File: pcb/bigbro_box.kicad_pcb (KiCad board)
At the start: 2 copper layers, 100 x 58 mm, 54 parts, among them J1 Current Sense, J2 Display, J3 Mains, J4 Debug, J5 RFID, J6 Relay, J7 Ext, K1 G5LE-1, Q1 MMBT3904, Q2 MMBT3904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

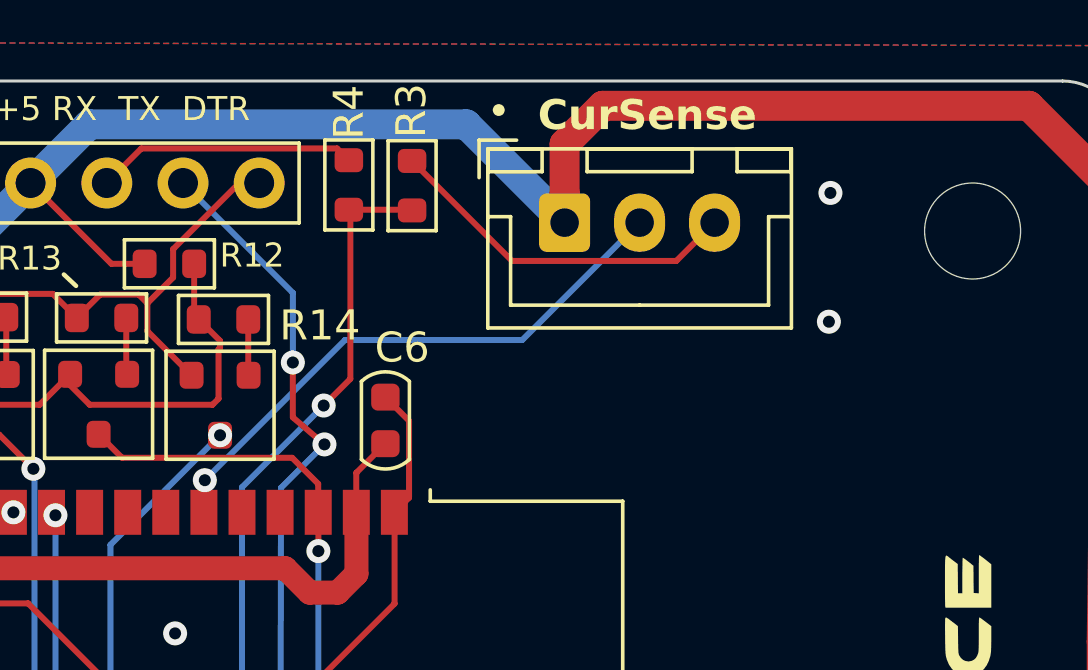
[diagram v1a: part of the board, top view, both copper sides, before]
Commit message: Add resistor divider for current sense input.
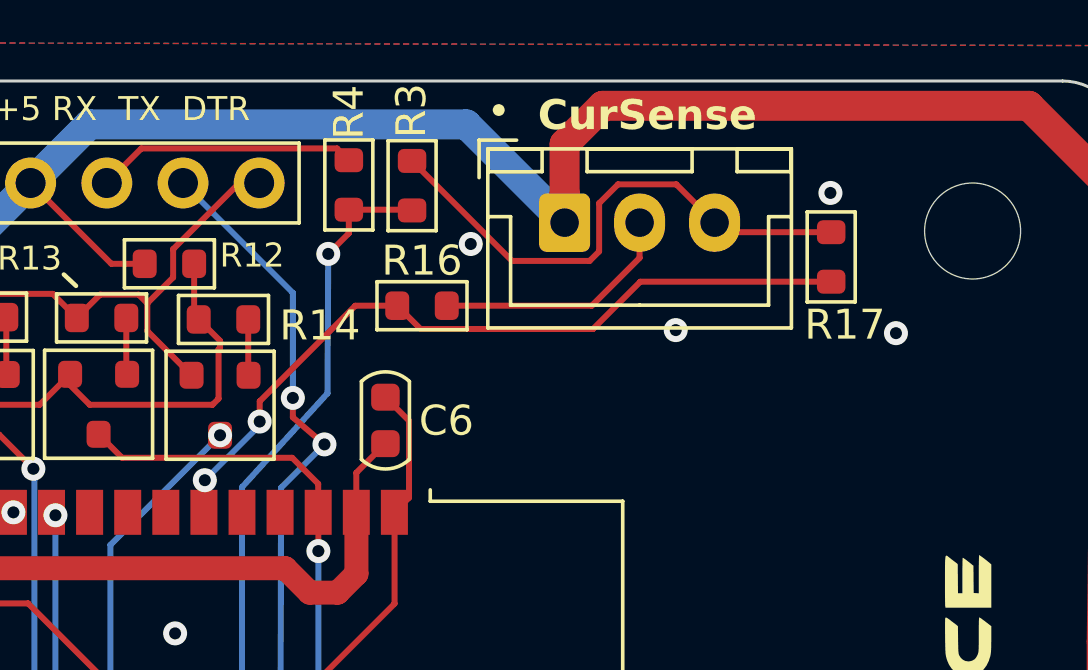
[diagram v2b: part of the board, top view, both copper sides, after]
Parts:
- added R16: 1k2, PCM_Resistor_SMD_AKL:R_0603_1608Metric, F.Cu at (142.6, 64.5)
- added R17: 2k2, PCM_Resistor_SMD_AKL:R_0603_1608Metric, F.Cu at (156.3, 62.9)
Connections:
- J1 pad 2: SENSE -> Net-(J1-Pin_2)
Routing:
- net Net-(J1-Pin_2): track 0.00 -> 8.26 mm
- net SENSE: track 19.1 -> 25.8 mm, vias 1 -> 2
- net GND: track 259.8 -> 265.8 mm, vias 29 -> 31

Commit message: Use zener.
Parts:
- removed R17: 2k2, PCM_Resistor_SMD_AKL:R_0603_1608Metric
- added D4: 3V0, Diode_SMD:D_MiniMELF, F.Cu at (156.1, 62.2)
- R16: value 1k2 -> 1k
- moved J1 0.59 mm to (146.8, 61.6)
- moved R16 0.51 mm to (142.1, 64.5)

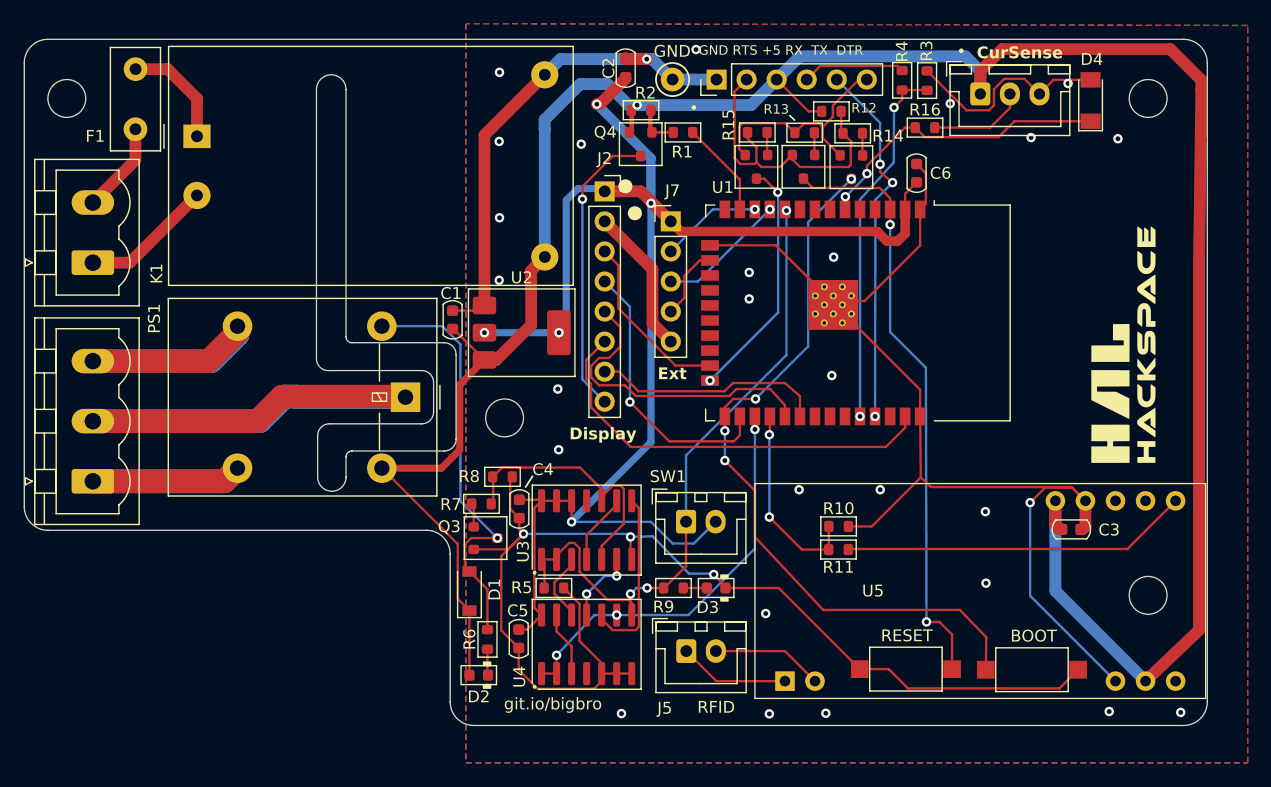
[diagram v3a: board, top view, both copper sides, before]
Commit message: Simplify debug circuitry.
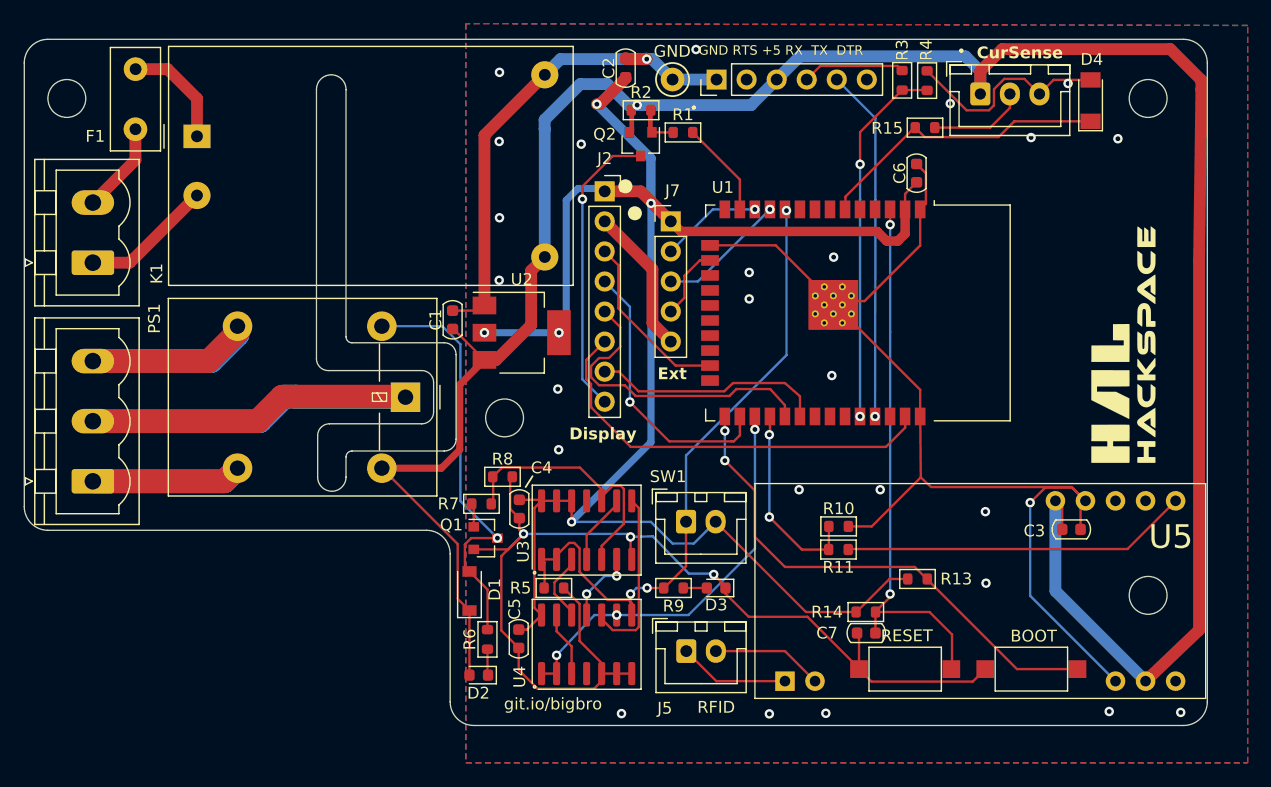
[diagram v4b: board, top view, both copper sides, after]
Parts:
- removed the Q1 at (135.9, 67.8)
- removed the Q2 at (131.9, 67.8)
- removed Q5: MMBT3904, PCM_Package_TO_SOT_SMD_AKL:SOT-23
- removed R12: 4k7, PCM_Resistor_SMD_AKL:R_0603_1608Metric
- removed the R15 at (128.0, 64.9)
- added C7: 100n, Capacitor_SMD_AKL:C_0603_1608Metric, F.Cu at (137.2, 107.2)
- C1, C2, C3, C4, C5, C6: footprint PCM_Capacitor_SMD_AKL:C_0603_1608Metric -> Capacitor_SMD_AKL:C_0603_1608Metric
- D2, D3: footprint PCM_LED_SMD_AKL:LED_0603_1608Metric -> LED_SMD:LED_0603_1608Metric
- Q1: renamed from Q3; footprint PCM_Package_TO_SOT_SMD_AKL:SOT-23 -> Package_TO_SOT_SMD:SOT-23
- Q2: renamed from Q4; footprint PCM_Package_TO_SOT_SMD_AKL:SOT-23 -> Package_TO_SOT_SMD:SOT-23
- R1, R10, R11, R2, R3, R4, R5, R6, R7, R8, R9: footprint PCM_Resistor_SMD_AKL:R_0603_1608Metric -> Resistor_SMD_AKL:R_0603_1608Metric
- R13, R14: value 1k -> 10k; footprint PCM_Resistor_SMD_AKL:R_0603_1608Metric -> Resistor_SMD_AKL:R_0603_1608Metric
- R15: renamed from R16; footprint PCM_Resistor_SMD_AKL:R_0603_1608Metric -> Resistor_SMD_AKL:R_0603_1608Metric
- U2: footprint PCM_Package_TO_SOT_SMD_AKL:SOT-223-3_TabPin2 -> Package_TO_SOT_SMD:SOT-223-3_TabPin2
- moved R14 40.5 mm to (137.1, 105.4), turned to 0 degrees
- moved R13 38.9 mm to (141.5, 102.6)
- moved SW2 10.7 mm to (140.5, 110.2), turned to 0 degrees
- moved SW3 10.6 mm to (151.1, 110.2)
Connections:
- J4 pad 2: ~{RTS} -> unconnected-(J4-Pin_2-Pad2)
- J4 pad 6: ~{DTR} -> unconnected-(J4-Pin_6-Pad6)
- R13 pad 1: Net-(Q2-B) (its old number) -> ~{BOOT}
- R13 pad 2: ~{DTR} -> +3V3
- R14 pad 1: Net-(Q1-B) -> +3V3
- R14 pad 2: ~{RTS} -> ~{RESET}
- SW2 pad 2: ~{BOOT} -> ~{RESET}
- SW3 pad 2: ~{RESET} -> ~{BOOT}
- U1 pad 24: IO2 -> unconnected-(U1-IO2-Pad24)
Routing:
- net ~{RTS}: track 26.2 -> 0.00 mm
- net IO2: track 20.6 -> 0.00 mm, vias 2 -> 0
- net +3V3: track 131.6 -> 152.2 mm
- net ~{BOOT}: track 63.1 -> 43.4 mm, vias 4 -> 2
- net ~{DTR}: track 19.5 -> 0.00 mm
- net +5V: track 210.0 -> 205.1 mm
- net GND: track 265.9 -> 261.1 mm, vias 31 -> 30
- net ~{RESET}: track 50.6 -> 46.4 mm
- net Net-(Q5-B): track 1.93 -> 0.00 mm
- net Net-(Q2-B) (its old number): track 1.89 -> 0.00 mm
- net Net-(Q1-B): track 1.87 -> 0.00 mm
- net TX: track 31.1 -> 29.8 mm, vias 3 -> 1
- net unconnected-(J4-Pin_6-Pad6): track 0.00 -> 0.66 mm
- net SENSE: track 26.0 -> 25.5 mm, vias 2 -> 0

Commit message: Add power LEDs.
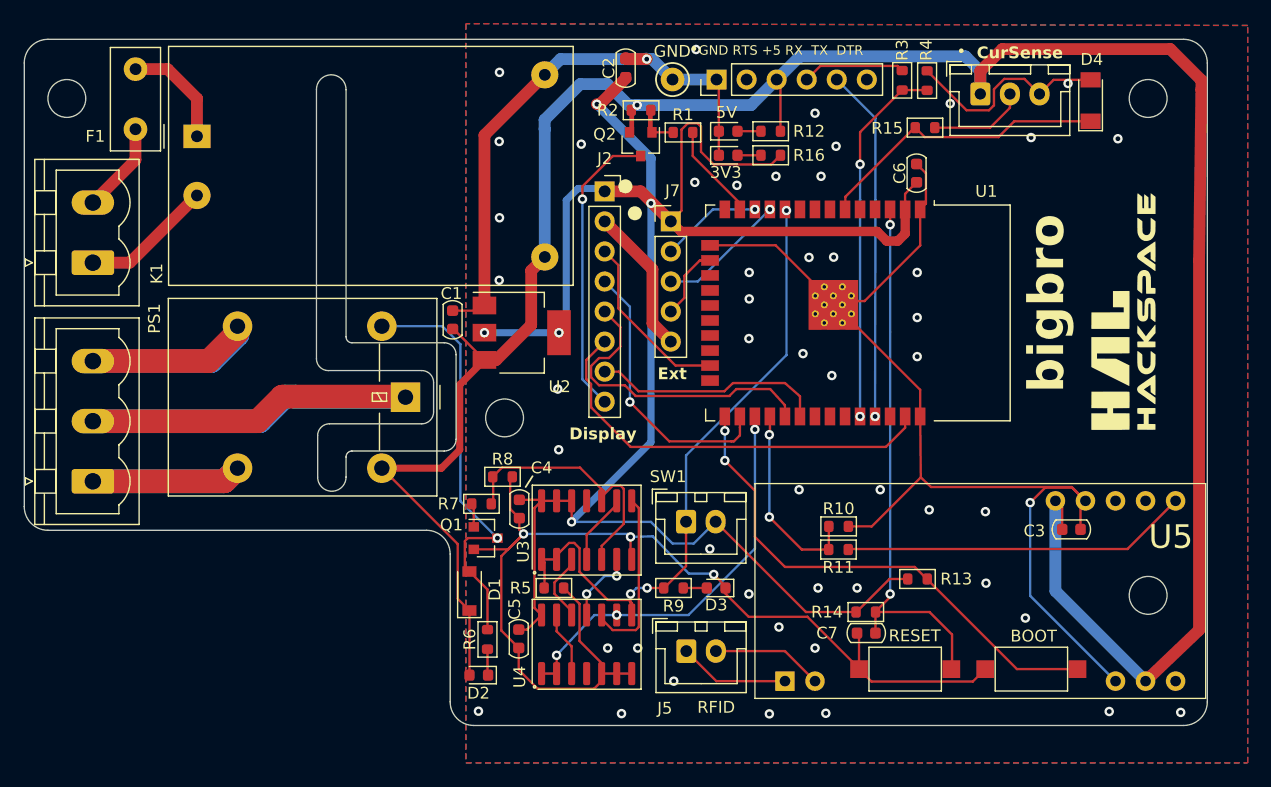
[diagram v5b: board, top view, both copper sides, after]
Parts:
- added D5: LED, LED_SMD:LED_0603_1608Metric, F.Cu at (125.5, 64.8)
- added D6: LED, LED_SMD:LED_0603_1608Metric, F.Cu at (125.5, 66.8)
- added R12: 3k3, Resistor_SMD_AKL:R_0603_1608Metric, F.Cu at (129.1, 64.8)
- added R16: 1k5, Resistor_SMD_AKL:R_0603_1608Metric, F.Cu at (129.1, 66.8)
- moved G*** 2.79 mm to (158.9, 80.0)
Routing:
- net +3V3: track 152.2 -> 171.9 mm
- net GND: track 261.1 -> 267.6 mm, vias 30 -> 54
- net +5V: track 205.1 -> 209.6 mm
- net Net-(D6-A): track 0.00 -> 1.98 mm
- net Net-(D5-A): track 0.00 -> 1.98 mm
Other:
- board text added: "3V3"
- board text added: "5V"
- board text added: "bigbro"
- board text removed: "git.io/bigbro"
